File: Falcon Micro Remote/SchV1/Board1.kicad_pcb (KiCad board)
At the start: 2 copper layers, 37 parts, among them J51 Conn_01x03_Male, SW31 SW_Push, SW51 SW_Push, SW61 SW_Push, SW62 SW_Push, SW63 SW_Push, SW64 SW_Push, SW71 SW_Push, SW72 SW_Push, SW73 SW_Push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

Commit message: Made modifications to sch and brd files
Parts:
- added D41: SS34, Diode_SMD:D_SMA, F.Cu at (175.2, 84.1)
- added J41: Conn_01x02_Male, Connector_PinSocket_2.54mm:PinSocket_1x02_P2.54mm_Vertical, F.Cu at (184.6, 85.1)
- added R41: 20K, Resistor_SMD:R_0402_1005Metric, F.Cu at (172.8, 88.7)
- added R42: 1K, Resistor_SMD:R_0402_1005Metric, F.Cu at (177.2, 88.7)
- R81, R82: value 200 -> 205
- moved D82 85.9 mm to (81.4, 65.2), turned to -90 degrees
- moved SW64 84.2 mm to (95.4, 85.2)
- moved SW62 82.9 mm to (82.7, 75.5)
- moved D81 81.7 mm to (85.3, 65.2), turned to -90 degrees
- moved SW61 81.6 mm to (95.4, 65.9)
- moved R81 77.7 mm to (85.3, 68.7), turned to 90 degrees
- moved R82 73.0 mm to (81.4, 68.7), turned to 90 degrees
- moved C41 56.1 mm to (117.0, 68.8), turned to 180 degrees
- moved R61 55.6 mm to (117.0, 78.2), turned to 180 degrees
- moved SW63 47.8 mm to (108.0, 75.6)
- moved SW51 46.5 mm to (108.2, 85.3)
- moved C31 45.8 mm to (117.0, 75.8)
- moved J51 44.3 mm to (146.7, 84.9), turned to 180 degrees
- moved C42 42.6 mm to (117.0, 73.5)
- moved R31 40.3 mm to (117.0, 71.2)
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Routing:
- net LED1: track 0.00 -> 76.1 mm
- net 3.3V: track 0.00 -> 64.1 mm
- net LED2: track 0.00 -> 22.9 mm
- net R2: track 0.00 -> 18.1 mm
- net R1: track 0.00 -> 17.7 mm
- net RT: track 0.00 -> 17.5 mm
- net LT: track 0.00 -> 8.00 mm
- net L2: track 0.00 -> 8.00 mm
- net L1: track 0.00 -> 8.00 mm
- net VIN: track 0.00 -> 3.34 mm
- net BOOT: track 0.00 -> 2.82 mm
- net Net-(D81-Pad2): track 0.00 -> 2.68 mm
- net Net-(D82-Pad2): track 0.00 -> 2.65 mm
- net TX: track 0.00 -> 0.78 mm
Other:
- board outline added: 112.8 x 31.6 mm

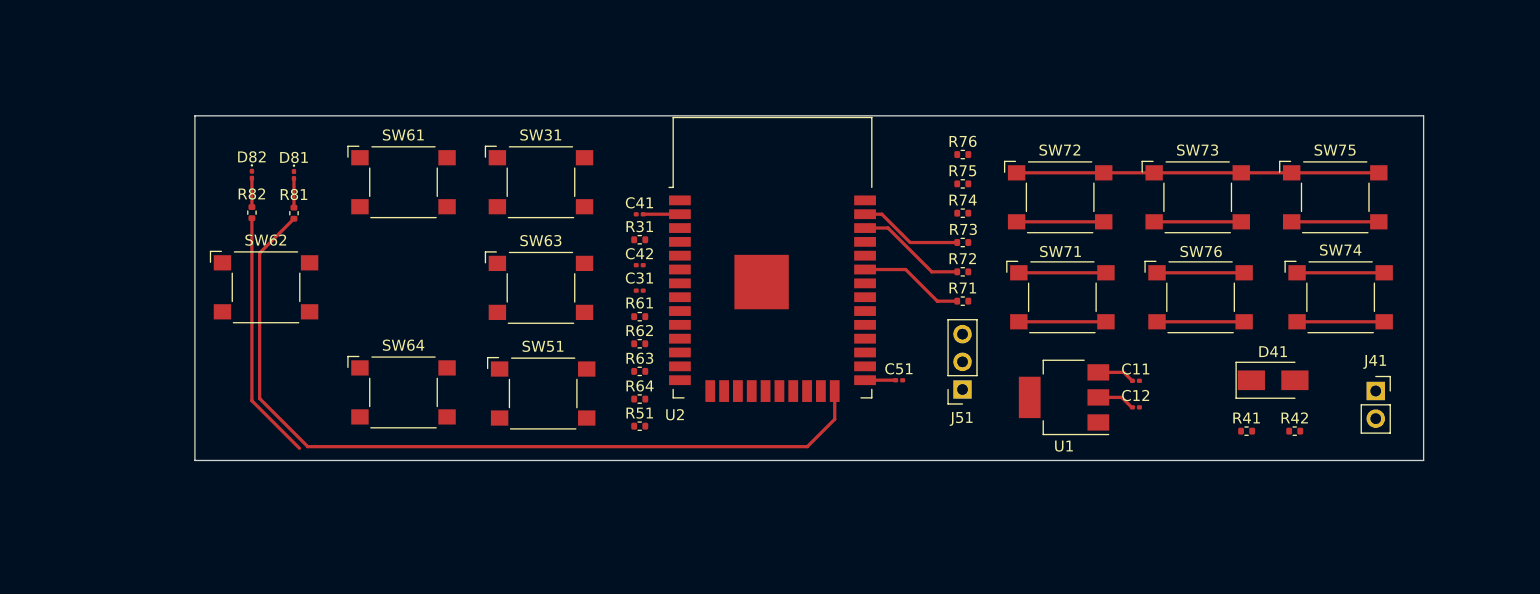
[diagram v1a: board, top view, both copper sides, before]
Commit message: Remote V1 has been sent for fabrication, fab project completed Will start on falcon Mini Lab V3, and Remote V2 next iteration
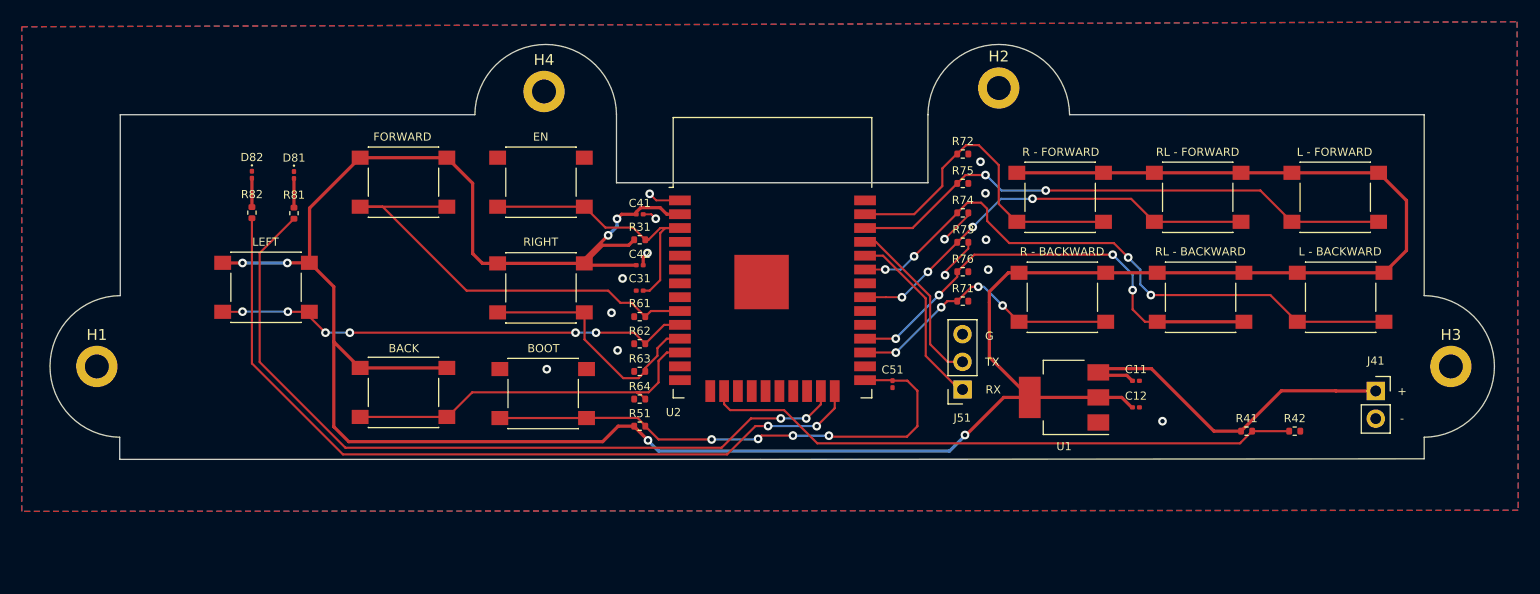
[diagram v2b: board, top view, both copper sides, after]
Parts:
- removed D41: SS34, Diode_SMD:D_SMA
- added H1: MountingHole_Pad, MountingHole:MountingHole_2.2mm_M2_DIN965_Pad, F.Cu at (67.2, 82.8)
- added H2: MountingHole_Pad, MountingHole:MountingHole_2.2mm_M2_DIN965_Pad, F.Cu at (150.0, 57.2)
- added H3: MountingHole_Pad, MountingHole:MountingHole_2.2mm_M2_DIN965_Pad, F.Cu at (191.5, 82.8)
- added H4: MountingHole_Pad, MountingHole:MountingHole_2.2mm_M2_DIN965_Pad, F.Cu at (108.3, 57.6)
- SW31, SW51, SW61, SW62, SW63, SW64, SW71, SW72, SW73, SW74, SW75, SW76: footprint Button_Switch_SMD:SW_SPST_Omron_B3FS-100xP -> Button_Switch_SMD:SW_SPST_PTS645
- moved R72 10.8 mm to (146.7, 63.3)
- moved R76 10.8 mm to (146.7, 74.1)
- moved C51 0.71 mm to (140.3, 84.4), turned to 90 degrees
- turned C41 to 0 degrees
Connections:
- J41 pad 1: BMS -> VIN
- R41 pad 1: BMS -> VIN
- R61 pad 1: F -> 33
- R62 pad 1: B -> 25
- R63 pad 1: L -> 26
- R64 pad 1: R -> 27
- R71 pad 1: R1 -> 16
- R72 pad 1: R2 -> 23
- R73 pad 1: RT -> 19
- R74 pad 1: L1 -> 21
- R75 pad 1: L2 -> 22
- R76 pad 1: LT -> 17
- SW61 pad 2: F -> 33
- SW62 pad 2: B -> 25
- SW63 pad 2: L -> 26
- SW64 pad 2: R -> 27
- SW71 pad 2: R1 -> 16
- SW72 pad 2: R2 -> 23
- SW73 pad 2: RT -> 19
- SW74 pad 2: L1 -> 21
- SW75 pad 2: L2 -> 22
- SW76 pad 2: LT -> 17
- U2 pad 10: L1 -> 25
- U2 pad 11: L2 -> 26
- U2 pad 12: L3 -> 27
- U2 pad 16: unconnected-(U2-Pad16) -> B+
- U2 pad 23: unconnected-(U2-Pad23) -> LED1
- U2 pad 24: LED1 -> LED2
- U2 pad 27: F -> 16
- U2 pad 28: B -> 17
- U2 pad 30: L -> 18
- U2 pad 31: R -> 19
- U2 pad 33: R1 -> 21
- U2 pad 36: R2 -> 22
- U2 pad 37: RT -> 23
- U2 pad 8: B+ -> 32
- U2 pad 9: unconnected-(U2-Pad9) -> 33
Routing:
- net 3.3V: track 64.1 -> 267.9 mm, vias 0 -> 6
- net 21: track 0.00 -> 56.2 mm, vias 0 -> 4
- net B+: track 0.00 -> 55.0 mm
- net 22: track 0.00 -> 51.0 mm, vias 0 -> 2
- net LED2: track 22.9 -> 73.7 mm, vias 0 -> 2
- net BOOT: track 2.82 -> 48.2 mm, vias 0 -> 4
- net 25: track 0.00 -> 44.2 mm, vias 0 -> 6
- net 17: track 0.00 -> 42.7 mm, vias 0 -> 4
- net 33: track 0.00 -> 41.8 mm
- net 19: track 0.00 -> 39.2 mm, vias 0 -> 4
- net 27: track 0.00 -> 34.0 mm
- net 23: track 0.00 -> 30.5 mm
- net VIN: track 3.34 -> 32.9 mm
- net EN: track 0.00 -> 26.7 mm
- net 16: track 0.00 -> 26.0 mm, vias 0 -> 4
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- added copper zone on B.Cu, net GND
- added copper zone on F.Cu, net GND
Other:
- board size 112.8 x 31.6 mm -> 132.6 x 38.1 mm
- board text added: "+"
- board text added: "-"
- board text added: "BACK"
- board text added: "BOOT"
- board text added: "EN"
- board text added: "FORWARD"
- board text added: "G"
- board text added: "L - BACKWARD"
- board text added: "L - FORWARD"
- board text added: "LEFT"
- board text added: "R - BACKWARD"
- board text added: "R - FORWARD"
- board text added: "RIGHT"
- board text added: "RL - BACKWARD"
- board text added: "RL - FORWARD"
- board text added: "RX"
- board text added: "TX"
